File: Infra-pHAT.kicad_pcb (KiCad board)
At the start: 2 copper layers, 65 x 30 mm, 24 parts, among them Q1 BC817, U1 CAT24C32WI-GT3

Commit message: Infra-pHAT.kicad_pcb: Route for IR RX
Signed-off-by: Leon Anavi <leon@anavi.org>
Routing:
- net Net-(IRRX1-Pad1): track 0.00 -> 43.5 mm, vias 0 -> 1
- net +3V3: track 94.7 -> 108.3 mm
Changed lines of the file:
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@@
   (general
     (links 59)
-    (no_connects 14)
-    (area 148.451099 74.953599 213.551101 105.053601)
+    (no_connects 12)
+    (area 136.779 73.66 225.171 106.426)
     (thickness 1.6)
     (drawings 13)
-    (tracks 277)
+    (tracks 297)
     (zones 0)
     (modules 24)
@@
   (gr_arc (start 151.5011 102.0036) (end 148.5011 102.0036) (angle -90) (layer Edge.Cuts) (width 0.1))
   (gr_circle (center 152.0011 101.5036) (end 152.0011 101.5036) (layer Edge.Cuts) (width 0.1))
+  (segment (start 156.718 79.502) (end 156.757 79.495) (width 0.5) (layer B.Cu) (net 1) (status 80000))
+  (segment (start 156.718 79.756) (end 156.718 79.502) (width 0.5) (layer B.Cu) (net 1) (status 80000))
+  (segment (start 157.861 80.899) (end 156.718 79.756) (width 0.5) (layer B.Cu) (net 1) (status 80000))
+  (segment (start 161.417 80.899) (end 157.861 80.899) (width 0.5) (layer B.Cu) (net 1) (status 80000))
+  (segment (start 162.179 81.661) (end 161.417 80.899) (width 0.5) (layer B.Cu) (net 1) (status 80000))
+  (segment (start 162.433 81.661) (end 162.179 81.661) (width 0.5) (layer B.Cu) (net 1) (status 80000))
+  (segment (start 165.227 84.455) (end 162.433 81.661) (width 0.5) (layer B.Cu) (net 1) (status 80000))
+  (segment (start 165.227 84.582) (end 165.227 84.455) (width 0.5) (layer B.Cu) (net 1) (status 80000))
+  (segment (start 167.132 86.487) (end 165.227 84.582) (width 0.5) (layer B.Cu) (net 1) (status 80000))
+  (segment (start 167.1 86.5) (end 167.132 86.487) (width 0.5) (layer B.Cu) (net 1) (status 80000))
   (segment (start 169.33 90.46) (end 169.291 90.424) (width 0.5) (layer F.Cu) (net 1) (status 80000))
   (segment (start 169.291 90.424) (end 168.783 90.424) (width 0.5) (layer F.Cu) (net 1) (status 80000))
@@
   (segment (start 183.261 86.487) (end 183.261 91.567) (width 0.5) (layer F.Cu) (net 11) (status 80000))
   (segment (start 183.261 91.567) (end 183.3 91.56) (width 0.5) (layer F.Cu) (net 11) (status 80000))
+  (segment (start 160.186 102.101) (end 160.147 102.108) (width 0.5) (layer B.Cu) (net 14) (status 80000))
+  (segment (start 160.147 102.108) (end 156.464 98.425) (width 0.5) (layer B.Cu) (net 14) (status 80000))
+  (segment (start 156.464 98.425) (end 156.464 86.614) (width 0.5) (layer B.Cu) (net 14) (status 80000))
+  (via (at 156.464 86.614) (size 0.85) (layers F.Cu B.Cu) (net 14) (status 80000))
+  (segment (start 156.464 86.614) (end 155.321 85.471) (width 0.5) (layer F.Cu) (net 14) (status 80000))
+  (segment (start 155.321 85.471) (end 155.321 75.565) (width 0.5) (layer F.Cu) (net 14) (status 80000))
+  (segment (start 155.321 75.565) (end 168.402 75.565) (width 0.5) (layer F.Cu) (net 14) (status 80000))
+  (segment (start 168.402 75.565) (end 169.418 76.581) (width 0.5) (layer F.Cu) (net 14) (status 80000))
+  (segment (start 169.418 76.581) (end 169.418 76.962) (width 0.5) (layer F.Cu) (net 14) (status 80000))
+  (segment (start 169.418 76.962) (end 169.457 76.955) (width 0.5) (layer F.Cu) (net 14) (status 80000))
 )

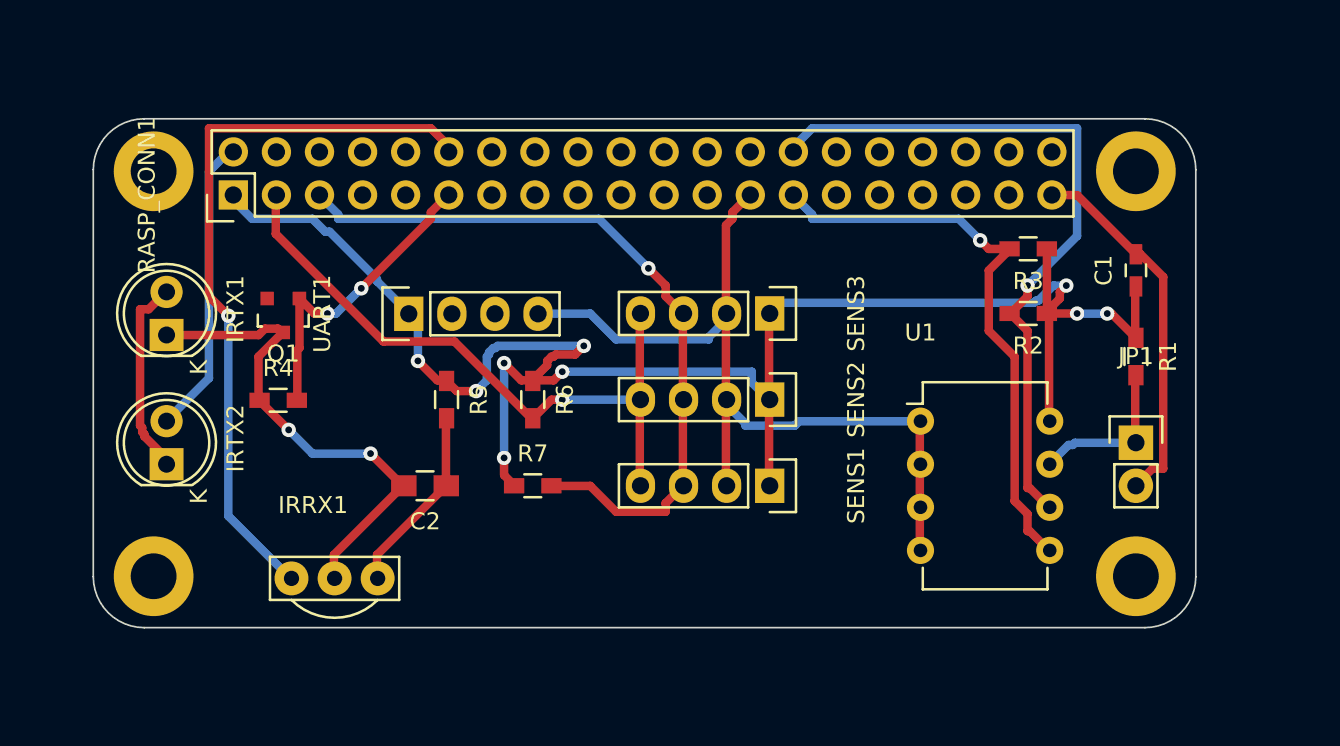
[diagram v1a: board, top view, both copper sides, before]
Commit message: Fix position of mounting holes and pin header
Fix wiring of transistor for IR leds

Signed-off-by: Rangel Ivanov <rangelivanov88@gmail.com>
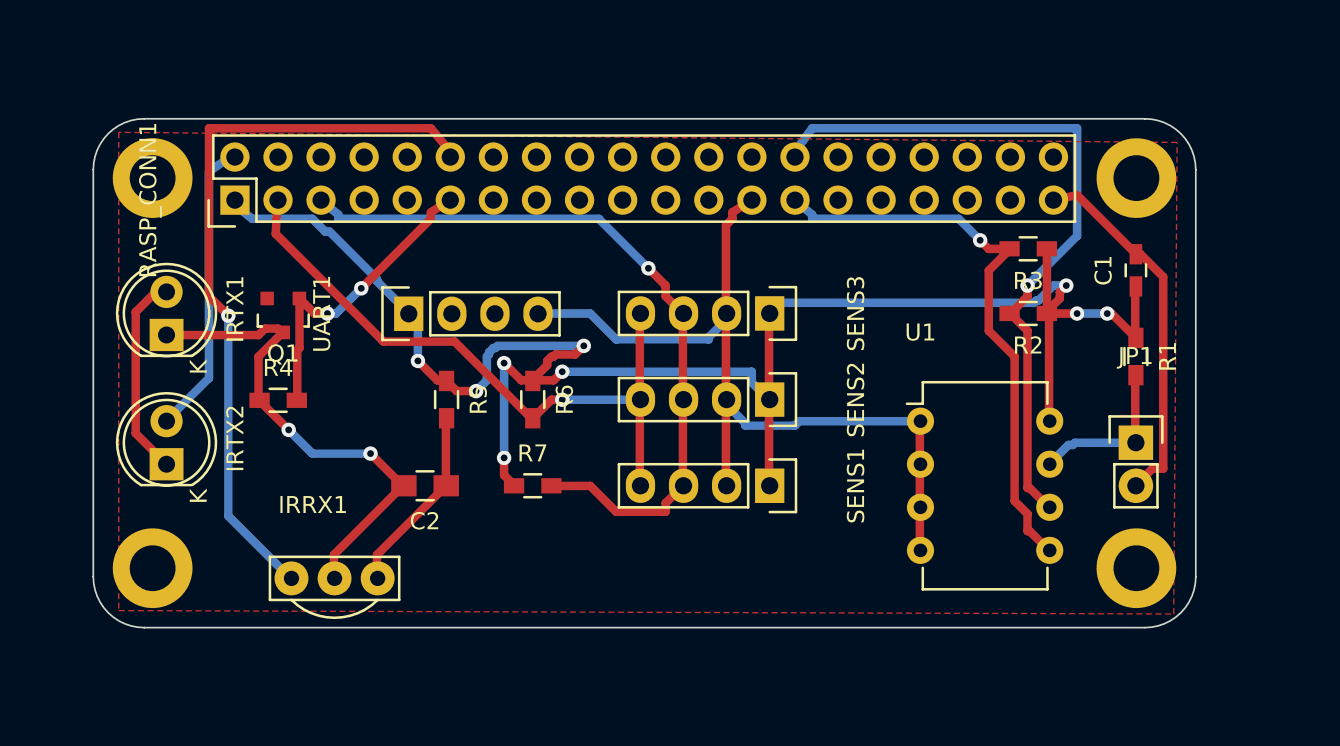
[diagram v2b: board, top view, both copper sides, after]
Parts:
- moved REF4 0.48 mm to (152.0, 101.5)
- moved REF3 0.47 mm to (210.0, 101.5)
- moved REF1 0.41 mm to (152.0, 78.5)
- moved REF2 0.40 mm to (210.0, 78.5)
- moved RASP_CONN1 0.32 mm to (156.8, 79.8)
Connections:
- IRTX1 pad 1: GND -> Net-(IRTX1-Pad1)
- Q1 pad 2: (no net) -> GND
- Q1 pad 3: GND -> Net-(IRTX1-Pad1)
- RASP_CONN1 pad 13: (no net) -> Net-(RASP_CONN1-Pad13)
- RASP_CONN1 pad 15: (no net) -> Net-(RASP_CONN1-Pad15)
- RASP_CONN1 pad 16: (no net) -> Net-(RASP_CONN1-Pad16)
- RASP_CONN1 pad 18: (no net) -> Net-(RASP_CONN1-Pad18)
- RASP_CONN1 pad 19: (no net) -> Net-(RASP_CONN1-Pad19)
- RASP_CONN1 pad 21: (no net) -> Net-(RASP_CONN1-Pad21)
- RASP_CONN1 pad 22: (no net) -> Net-(RASP_CONN1-Pad22)
- RASP_CONN1 pad 23: (no net) -> Net-(RASP_CONN1-Pad23)
- RASP_CONN1 pad 24: (no net) -> Net-(RASP_CONN1-Pad24)
- RASP_CONN1 pad 26: (no net) -> Net-(RASP_CONN1-Pad26)
- RASP_CONN1 pad 29: (no net) -> Net-(RASP_CONN1-Pad29)
- RASP_CONN1 pad 31: (no net) -> Net-(RASP_CONN1-Pad31)
- RASP_CONN1 pad 32: (no net) -> Net-(RASP_CONN1-Pad32)
- RASP_CONN1 pad 33: (no net) -> Net-(RASP_CONN1-Pad33)
- RASP_CONN1 pad 35: (no net) -> Net-(RASP_CONN1-Pad35)
- RASP_CONN1 pad 36: (no net) -> Net-(RASP_CONN1-Pad36)
- RASP_CONN1 pad 37: (no net) -> Net-(RASP_CONN1-Pad37)
- RASP_CONN1 pad 38: (no net) -> Net-(RASP_CONN1-Pad38)
- RASP_CONN1 pad 40: (no net) -> Net-(RASP_CONN1-Pad40)
- RASP_CONN1 pad 7: (no net) -> Net-(RASP_CONN1-Pad7)
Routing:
- net GND: track 103.0 -> 93.6 mm
- net Net-(IRTX1-Pad1): track 0.00 -> 9.27 mm
- net Net-(IRTX1-Pad2): track 11.8 -> 12.5 mm
- added copper zone on F.Cu, net +3V3

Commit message: Add filled zone for front layer (GND net)
Route RX/TX for UART connector

Signed-off-by: Rangel Ivanov <rangelivanov88@gmail.com>
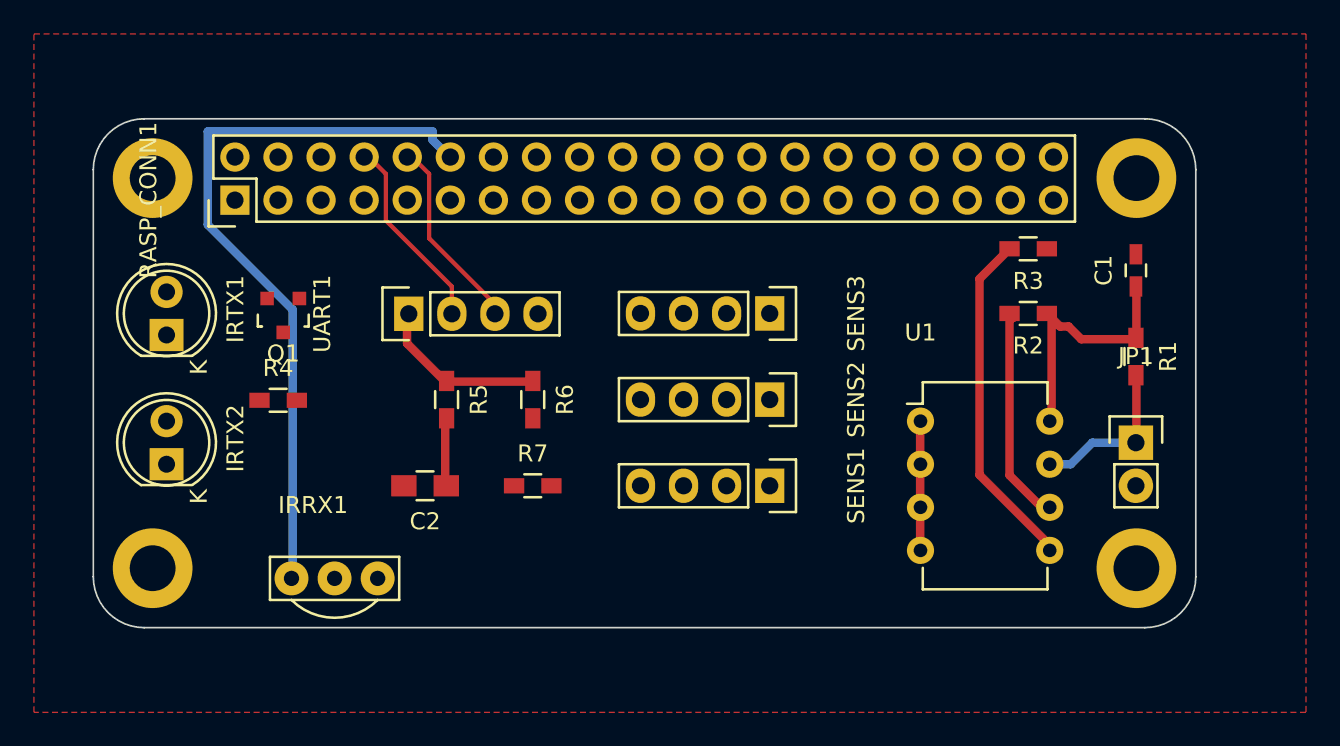
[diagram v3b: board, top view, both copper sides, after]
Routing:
- net GND: track 93.6 -> 8.40 mm, vias 2 -> 0
- net +3V3: track 108.1 -> 26.3 mm, vias 9 -> 0
- net Net-(R7-Pad2): track 44.4 -> 0.00 mm, vias 1 -> 0
- net Net-(R6-Pad2): track 39.0 -> 0.00 mm, vias 1 -> 0
- net Net-(R2-Pad2): track 42.8 -> 13.2 mm, vias 1 -> 0
- net Net-(Q1-Pad1): track 18.2 -> 0.00 mm, vias 2 -> 0
- net +5V: track 17.6 -> 0.00 mm
- net Net-(R3-Pad2): track 34.0 -> 20.4 mm, vias 1 -> 0
- net Net-(IRTX1-Pad2): track 12.5 -> 0.00 mm
- net /RXD: track 0.00 -> 11.6 mm
- net /TXD: track 0.00 -> 11.6 mm
- net Net-(IRTX1-Pad1): track 9.27 -> 0.00 mm
- net Net-(C2-Pad1): track 11.2 -> 4.25 mm
- net Net-(IRRX1-Pad1): track 43.8 -> 43.7 mm, vias 1 -> 0
- added copper zone on F.Cu, net GND
- removed copper zone on F.Cu, net +3V3

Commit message: Infra-pHAT.kicad_pcb: Update routing
Signed-off-by: Leon Anavi <leon@anavi.org>
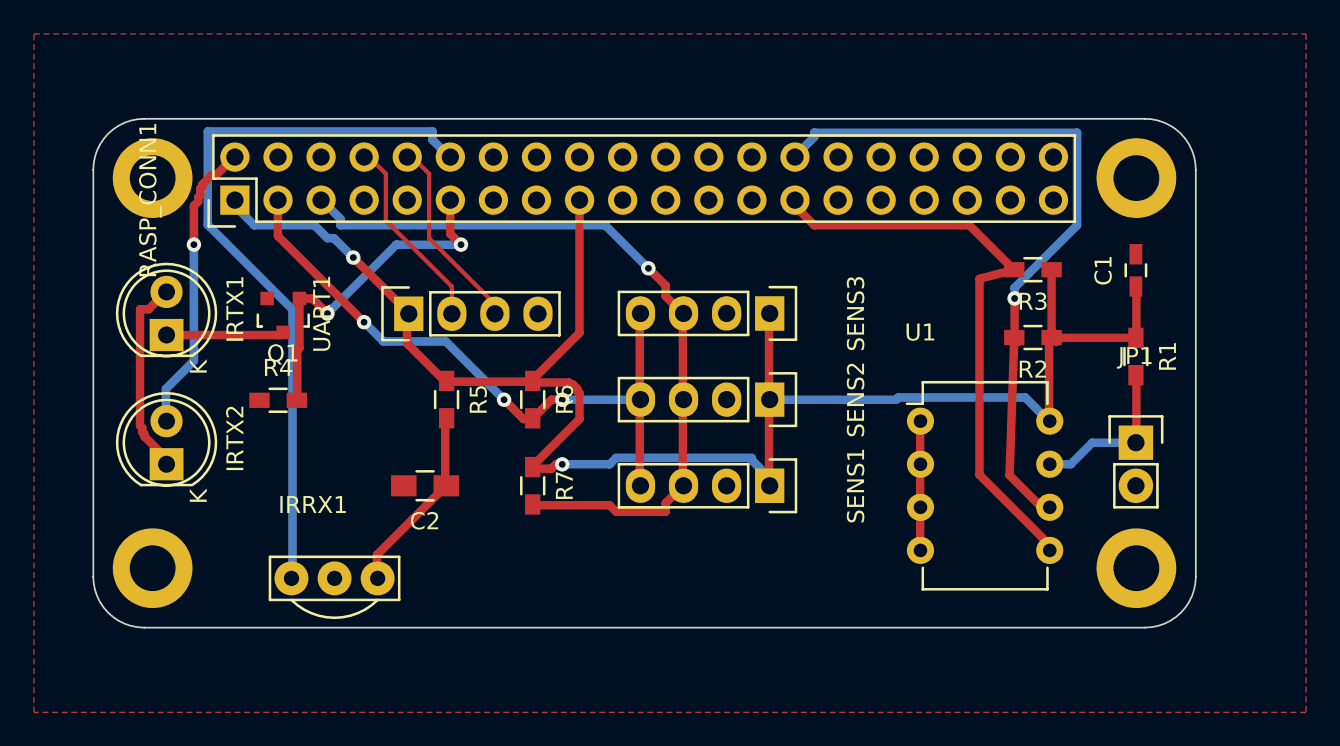
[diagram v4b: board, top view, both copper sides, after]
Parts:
- moved R2 1.45 mm to (203.9, 87.9)
- moved R3 1.26 mm to (203.9, 83.9)
- turned R7 to 270 degrees
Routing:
- net +3V3: track 26.3 -> 105.5 mm, vias 0 -> 2
- net Net-(R7-Pad2): track 0.00 -> 45.2 mm, vias 0 -> 1
- net Net-(R6-Pad2): track 0.00 -> 39.0 mm, vias 0 -> 3
- net Net-(R2-Pad2): track 13.2 -> 42.8 mm, vias 0 -> 1
- net Net-(Q1-Pad1): track 0.00 -> 20.6 mm, vias 0 -> 2
- net +5V: track 0.00 -> 17.5 mm, vias 0 -> 1
- net Net-(R3-Pad2): track 20.4 -> 35.1 mm
- net Net-(IRTX1-Pad2): track 0.00 -> 11.8 mm
- net Net-(C2-Pad1): track 4.25 -> 11.4 mm
- net Net-(IRTX1-Pad1): track 0.00 -> 7.02 mm

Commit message: Infra-pHAT.kicad_pcb: Silkscreen text added
Signed-off-by: Leon Anavi <leon@anavi.org>
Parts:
- renumbered UART1 to UART
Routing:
- added copper zone on B.Cu, net GND
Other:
- board text added: "3x I2C"
- board text added: "ANAVI Infra pHAT"
- board text added: "Made in Plovdiv, Bulgaria, EU"
- board text added: "SDA SCL GND 3.3V"
- board text added: "http://anavi.technology"
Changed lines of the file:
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@@
   (general
     (links 59)
-    (no_connects 3)
-    (area 136.779 66.294 225.171 110.109)
+    (no_connects 2)
+    (area 148.451099 74.953599 213.551101 105.053601)
     (thickness 1.6)
-    (drawings 15)
+    (drawings 20)
     (tracks 236)
     (zones 0)
@@
     (34 B.Paste user)
     (35 F.Paste user)
-    (36 B.SilkS user)
+    (36 B.SilkS user hide)
     (37 F.SilkS user)
     (38 B.Mask user)
@@
     (tags "capacitor 0603")
     (attr smd)
-    (fp_text reference C1 (at 0 -1.9 90) (layer F.SilkS)
+    (fp_text reference C1 (at -0.06 1.93 90) (layer F.SilkS)
       (effects (font (size 1 1) (thickness 0.15)))
     )
@@
     (tags "capacitor 0805")
     (attr smd)
-    (fp_text reference C2 (at 0 -2.1 180) (layer F.SilkS)
+    (fp_text reference C2 (at 3.71 -0.11 180) (layer F.SilkS)
       (effects (font (size 1 1) (thickness 0.15)))
     )
@@
     (fp_line (start -1.23 1.5) (end -1.23 -1.5) (layer F.SilkS) (width 0.15))
     (fp_circle (center 1.27 0) (end 0.97 -2.5) (layer F.SilkS) (width 0.15))
-    (fp_text user K (at -1.905 1.905 90) (layer F.SilkS)
+    (fp_text user K (at -1.905 1.905 90) (layer F.SilkS) hide
       (effects (font (size 1 1) (thickness 0.15)))
     )
@@
     (fp_line (start -1.23 1.5) (end -1.23 -1.5) (layer F.SilkS) (width 0.15))
     (fp_circle (center 1.27 0) (end 0.97 -2.5) (layer F.SilkS) (width 0.15))
-    (fp_text user K (at -1.905 1.905 90) (layer F.SilkS)
+    (fp_text user K (at -1.905 1.905 90) (layer F.SilkS) hide
       (effects (font (size 1 1) (thickness 0.15)))
     )
@@
     (descr "Through hole pin header")
     (tags "pin header")
-    (fp_text reference JP1 (at 0 -5.1) (layer F.SilkS)
+    (fp_text reference JP1 (at 2.63 1.3 90) (layer F.SilkS)
       (effects (font (size 1 1) (thickness 0.15)))
     )
@@
     (tags SOT-23)
     (attr smd)
-    (fp_text reference Q1 (at 0 -2.25 180) (layer F.SilkS)
+    (fp_text reference Q1 (at -2.75 -1.15 180) (layer F.SilkS)
       (effects (font (size 1 1) (thickness 0.15)))
     )
@@
     (tags "resistor 0603")
     (attr smd)
-    (fp_text reference R4 (at 0 -1.9) (layer F.SilkS)
+    (fp_text reference R4 (at 3.2 0.05) (layer F.SilkS)
       (effects (font (size 1 1) (thickness 0.15)))
     )
@@
     (tags "resistor 0603")
     (attr smd)
-    (fp_text reference R5 (at 0 -1.9 270) (layer F.SilkS)
+    (fp_text reference R5 (at 0.09 1.83 270) (layer F.SilkS)
       (effects (font (size 1 1) (thickness 0.15)))
     )
@@
     (tags "resistor 0603")
     (attr smd)
-    (fp_text reference R6 (at 0 -1.9 270) (layer F.SilkS)
+    (fp_text reference R6 (at 1.44 1.66 270) (layer F.SilkS)
       (effects (font (size 1 1) (thickness 0.15)))
     )
@@
     (tags "resistor 0603")
     (attr smd)
-    (fp_text reference R7 (at 0 -1.9 270) (layer F.SilkS)
+    (fp_text reference R7 (at 0.01 1.66 270) (layer F.SilkS)
       (effects (font (size 1 1) (thickness 0.15)))
     )
@@
     (descr "Through hole pin header")
     (tags "pin header")
-    (fp_text reference RASP_CONN1 (at 0 -5.1 90) (layer F.SilkS)
+    (fp_text reference RASP_CONN1 (at 0 -5.1 90) (layer F.SilkS) hide
       (effects (font (size 1 1) (thickness 0.15)))
     )
@@
     (descr "Through hole pin header")
     (tags "pin header")
-    (fp_text reference SENS1 (at 0 -5.1 270) (layer F.SilkS)
+    (fp_text reference SENS1 (at 0 -5.1 270) (layer F.SilkS) hide
       (effects (font (size 1 1) (thickness 0.15)))
     )
@@
     (descr "Through hole pin header")
     (tags "pin header")
-    (fp_text reference SENS2 (at 0 -5.1 270) (layer F.SilkS)
+    (fp_text reference SENS2 (at 0 -5.1 270) (layer F.SilkS) hide
       (effects (font (size 1 1) (thickness 0.15)))
     )
@@
     (descr "Through hole pin header")
     (tags "pin header")
-    (fp_text reference SENS3 (at 0 -5.1 270) (layer F.SilkS)
+    (fp_text reference SENS3 (at 0 -5.1 270) (layer F.SilkS) hide
       (effects (font (size 1 1) (thickness 0.15)))
     )
@@
     (descr "8-lead dip package, row spacing 7.62 mm (300 mils)")
     (tags "dil dip 2.54 300")
-    (fp_text reference U1 (at 0 -5.22) (layer F.SilkS)
+    (fp_text reference U1 (at 0 -5.22) (layer F.SilkS) hide
       (effects (font (size 1 1) (thickness 0.15)))
     )
@@
     (descr "Through hole pin header")
     (tags "pin header")
-    (fp_text reference UART1 (at 0 -5.1 90) (layer F.SilkS)
+    (fp_text reference UART (at -2.35 4.55 180) (layer F.SilkS)
       (effects (font (size 1 1) (thickness 0.15)))
     )
@@
   (module myfootprint:TSOP38X (layer F.Cu)
     (at 162.726 99.561)
-    (fp_text reference IRRX1 (at -1.27 -1.778) (layer F.SilkS)
+    (fp_text reference IRRX1 (at 0.074 0.339) (layer F.SilkS)
       (effects (font (size 1 1) (thickness 0.15)))
     )
@@
     (fp_circle (center 0 0) (end 2.6 0) (layer F.CrtYd) (width 0.05))
     (pad 4 thru_hole circle (at 0 0) (size 4.7 4.7) (drill 2.7) (layers *.Cu *.Mask F.SilkS))
+  )
+  (gr_text "3x I2C" (at 191.3 91.25 90) (layer F.SilkS)
+    (effects (font (size 1 1) (thickness 0.25)))
+  )
+  (gr_text "SDA SCL GND 3.3V" (at 184.75 83.9) (layer F.SilkS)
+    (effects (font (size 0.8 0.8) (thickness 0.125)))
+  )
+  (gr_text "Made in Plovdiv, Bulgaria, EU" (at 201.15 103.85) (layer F.SilkS)
+    (effects (font (size 0.5 0.5) (thickness 0.125)))
+  )
+  (gr_text http://anavi.technology (at 182.3 103.3) (layer F.SilkS)
+    (effects (font (size 1 1) (thickness 0.25)))
+  )
+  (gr_text "ANAVI Infra pHAT" (at 182.9 101) (layer F.SilkS)
+    (effects (font (size 1.5 1.5) (thickness 0.3)))
   )
   (dimension 3.5 (width 0.3) (layer F.CrtYd)
@@
   (segment (start 183.261 86.487) (end 182.245 85.471) (width 0.5) (layer F.Cu) (net 11) (status 80000))
   (segment (start 182.245 85.471) (end 182.245 84.836) (width 0.5) (layer F.Cu) (net 11) (status 80000))
-  (segment (start 182.245 84.836) (end 181.229 83.82) (width 0.5) (layer F.Cu) (net 11) (status 80000))
-  (via (at 181.229 83.82) (size 0.85) (layers F.Cu B.Cu) (net 11) (status 80000))
-  (segment (start 181.229 83.82) (end 178.689 81.28) (width 0.5) (layer B.Cu) (net 11) (status 80000))
+  (segment (start 182.245 84.836) (end 179.65 82.25) (width 0.5) (layer F.Cu) (net 11) (status 80000))
+  (via (at 179.65 82.25) (size 0.85) (layers F.Cu B.Cu) (net 11) (status 80000))
+  (segment (start 179.65 82.25) (end 178.689 81.28) (width 0.5) (layer B.Cu) (net 11) (status 80000))
   (segment (start 178.689 81.28) (end 163.068 81.28) (width 0.5) (layer B.Cu) (net 11) (status 80000))
   (segment (start 163.068 81.28) (end 163.068 80.899) (width 0.5) (layer B.Cu) (net 11) (status 80000))
@@
     (connect_pads (clearance 0.508))
     (min_thickness 0.254)
+    (fill yes (arc_segments 16) (thermal_gap 0.508) (thermal_bridge_width 0.508))
+    (polygon
+      (pts
+        (xy 220 110) (xy 145 110) (xy 145 70) (xy 220 70)
+      )
+    )
+  )
+  (zone (net 2) (net_name GND) (layer B.Cu) (hatch edge 0.508)
+    (connect_pads (clearance 0.508))
+    (min_thickness 0.254)
